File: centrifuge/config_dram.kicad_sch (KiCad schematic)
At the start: 4 parts

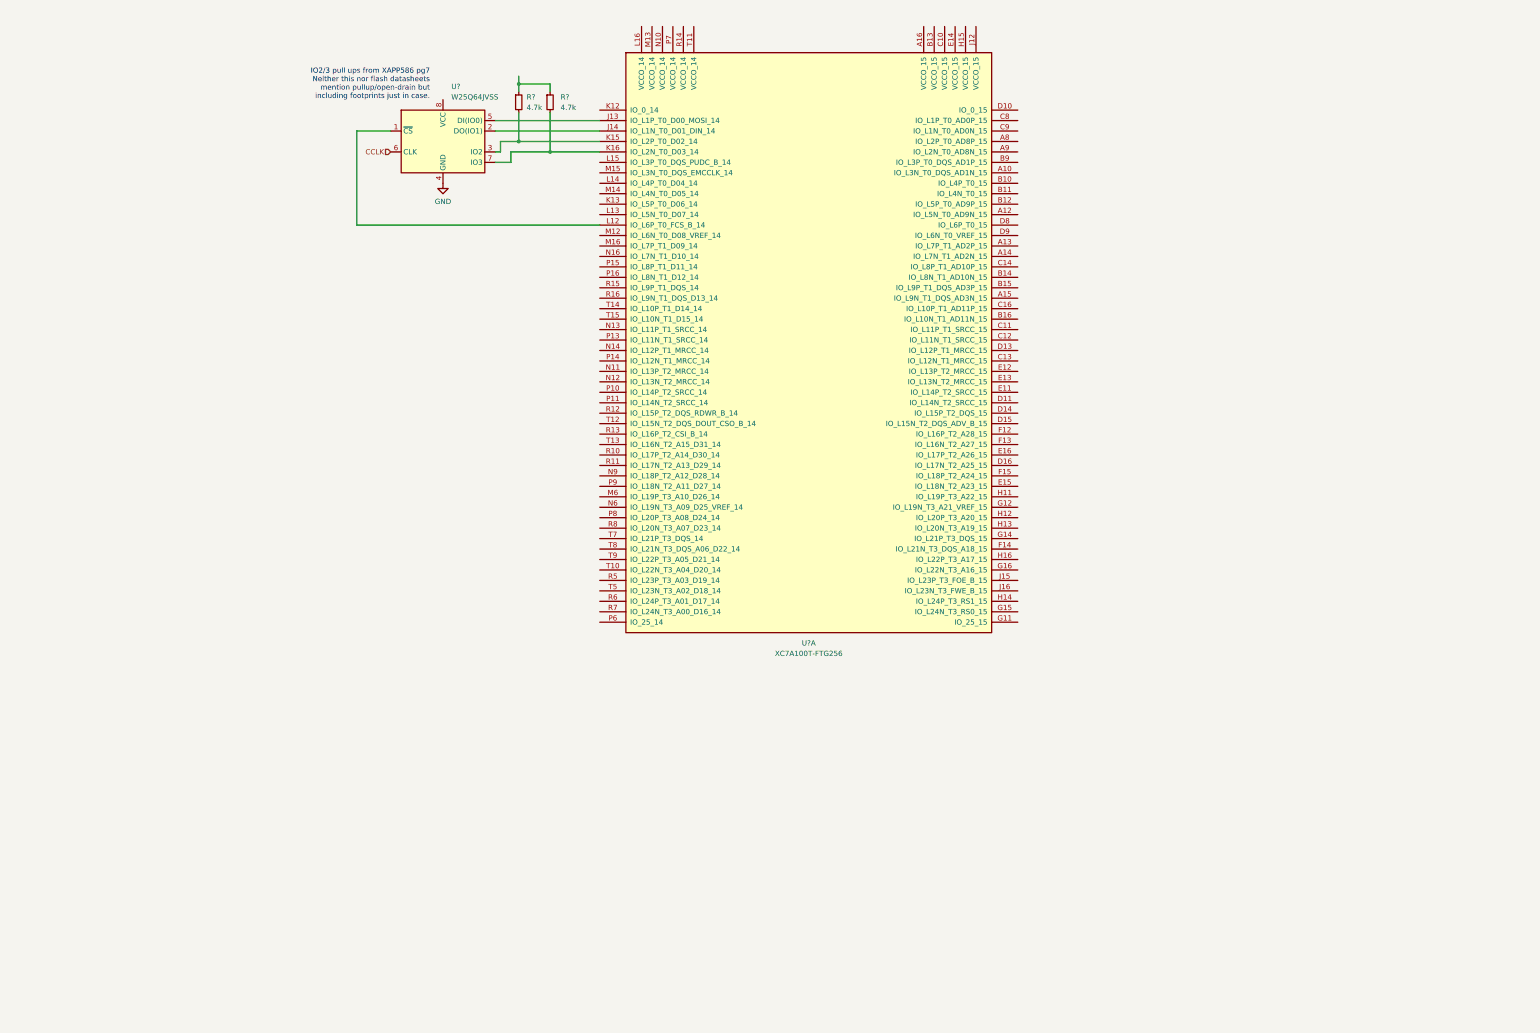
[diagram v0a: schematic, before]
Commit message: Made initial pin map of SRAM-FPGA and possible routing
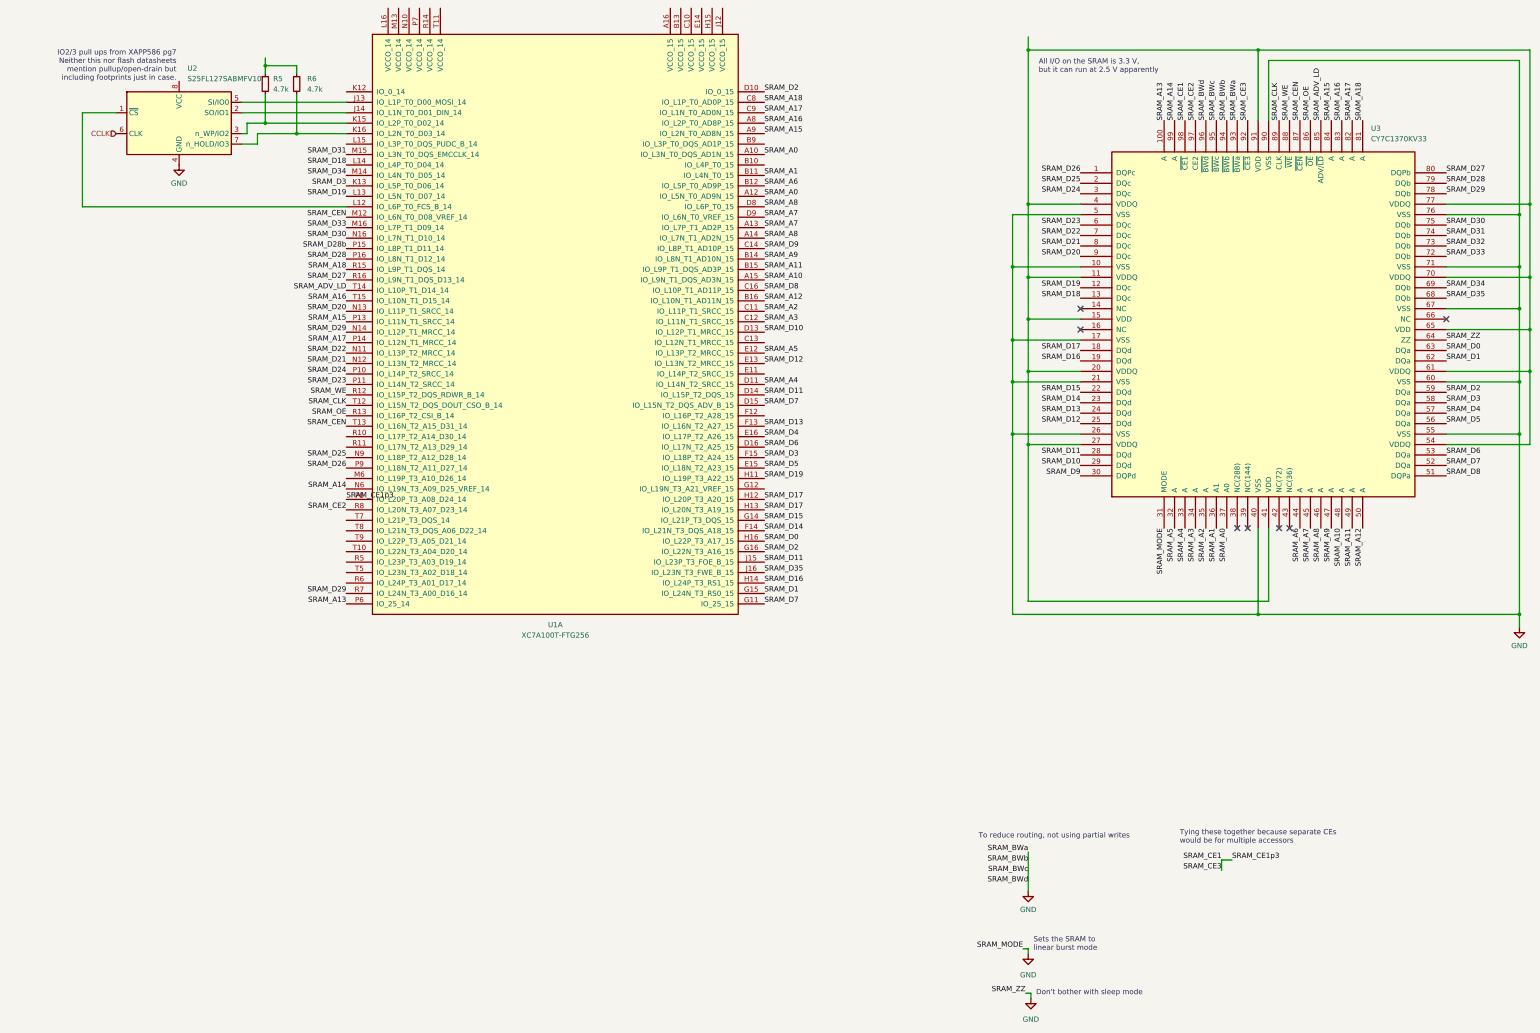
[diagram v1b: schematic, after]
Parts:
- added U3: CY7C1370KV33, Package_QFP:PQFP-100_14x20mm_P0.65mm, symbol centrifuge_symbols:CY7C1370KV33
- U1: renamed from U?; footprint (none) -> Package_BGA:Xilinx_FTG256
- U2: renamed from U?; value W25Q64JVSS -> S25FL127SABMFV10; symbol centrifuge_symbols:W25Q64JVSS -> centrifuge_symbols:S25FL127SABMFV10
- gave numbers to parts that had none: 2
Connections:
- net GND: now also U3.10 (VSS), U3.17 (VSS), U3.21 (VSS), U3.26 (VSS), U3.31 (MODE), U3.40 (VSS), U3.5 (VSS), U3.55 (VSS), U3.60 (VSS), U3.64 (ZZ), U3.67 (VSS), U3.71 (VSS), U3.76 (VSS), U3.90 (VSS), U3.93 (~{BWa}), U3.94 (~{BWb}), U3.95 (~{BWc}), U3.96 (~{BWd})
- net SRAM_A0: now reaches U1.A10 (IO_L3N_T0_DQS_AD1N_15)
- net SRAM_A0: now also U1.A12 (IO_L5N_T0_AD9N_15), U3.37 (A0)
- net SRAM_A7: now reaches U1.A13 (IO_L7P_T1_AD2P_15)
- net SRAM_A7: now also U1.D9 (IO_L6N_T0_VREF_15), U3.45 (A)
- net SRAM_A8: now reaches U1.A14 (IO_L7N_T1_AD2N_15)
- net SRAM_A8: now also U1.D8 (IO_L6P_T0_15), U3.46 (A)
- net SRAM_A10: now reaches U1.A15 (IO_L9N_T1_DQS_AD3N_15)
- net SRAM_A10: now also U3.48 (A)
- net SRAM_A16: now reaches U1.A8 (IO_L2P_T0_AD8P_15)
- net SRAM_A16: now also U1.T15 (IO_L10N_T1_D15_14), U3.83 (A)
- net SRAM_A15: now reaches U1.A9 (IO_L2N_T0_AD8N_15)
- net SRAM_A15: now also U1.P13 (IO_L11N_T1_SRCC_14), U3.84 (A)
- net SRAM_A1: now reaches U1.B11 (IO_L4N_T0_15)
- net SRAM_A1: now also U3.36 (A1)
- net SRAM_A6: now reaches U1.B12 (IO_L5P_T0_AD9P_15)
- net SRAM_A6: now also U3.44 (A)
- net SRAM_A9: now reaches U1.B14 (IO_L8N_T1_AD10N_15)
- net SRAM_A9: now also U3.47 (A)
- net SRAM_A11: now reaches U1.B15 (IO_L9P_T1_DQS_AD3P_15)
- net SRAM_A11: now also U3.49 (A)
- net SRAM_A12: now reaches U1.B16 (IO_L10N_T1_AD11N_15)
- net SRAM_A12: now also U3.50 (A)
- net SRAM_A2: now reaches U1.C11 (IO_L11P_T1_SRCC_15)
- net SRAM_A2: now also U3.35 (A)
- net SRAM_A3: now reaches U1.C12 (IO_L11N_T1_SRCC_15)
- net SRAM_A3: now also U3.34 (A)
- net SRAM_D9: now reaches U1.C14 (IO_L8P_T1_AD10P_15)
- net SRAM_D9: now also U3.30 (DQPd)
- net SRAM_D8: now reaches U1.C16 (IO_L10P_T1_AD11P_15)
- net SRAM_D8: now also U3.51 (DQPa)
- net SRAM_A18: now reaches U1.C8 (IO_L1P_T0_AD0P_15)
- net SRAM_A18: now also U1.R15 (IO_L9P_T1_DQS_14), U3.81 (A)
- net SRAM_A17: now reaches U1.C9 (IO_L1N_T0_AD0N_15)
- net SRAM_A17: now also U1.P14 (IO_L12N_T1_MRCC_14), U3.82 (A)
- net SRAM_D2: now reaches U1.D10 (IO_0_15)
- net SRAM_D2: now also U1.G16 (IO_L22N_T3_A16_15), U3.59 (DQa)
- net SRAM_A4: now reaches U1.D11 (IO_L14N_T2_SRCC_15)
- net SRAM_A4: now also U3.33 (A)
- net SRAM_D10: now reaches U1.D13 (IO_L12P_T1_MRCC_15)
- net SRAM_D10: now also U3.29 (DQd)
- net SRAM_D11: now reaches U1.D14 (IO_L15P_T2_DQS_15)
- net SRAM_D11: now also U1.J15 (IO_L23P_T3_FOE_B_15), U3.28 (DQd)
- net SRAM_D7: now reaches U1.D15 (IO_L15N_T2_DQS_ADV_B_15)
- net SRAM_D7: now also U1.G11 (IO_25_15), U3.52 (DQa)
- net SRAM_D6: now reaches U1.D16 (IO_L17N_T2_A25_15)
- net SRAM_D6: now also U3.53 (DQa)
- net SRAM_A5: now reaches U1.E12 (IO_L13P_T2_MRCC_15)
- net SRAM_A5: now also U3.32 (A)
- net SRAM_D12: now reaches U1.E13 (IO_L13N_T2_MRCC_15)
- net SRAM_D12: now also U3.25 (DQd)
- net SRAM_D5: now reaches U1.E15 (IO_L18N_T2_A23_15)
- net SRAM_D5: now also U3.56 (DQa)
- net SRAM_D4: now reaches U1.E16 (IO_L17P_T2_A26_15)
- net SRAM_D4: now also U3.57 (DQa)
- net SRAM_D13: now reaches U1.F13 (IO_L16N_T2_A27_15)
- net SRAM_D13: now also U3.24 (DQd)
- net SRAM_D14: now reaches U1.F14 (IO_L21N_T3_DQS_A18_15)
- net SRAM_D14: now also U3.23 (DQd)
- net SRAM_D3: now reaches U1.F15 (IO_L18P_T2_A24_15)
- net SRAM_D3: now also U1.K13 (IO_L5P_T0_D06_14), U3.58 (DQa)
- net SRAM_D15: now reaches U1.G14 (IO_L21P_T3_DQS_15)
- net SRAM_D15: now also U3.22 (DQd)
- net SRAM_D1: now reaches U1.G15 (IO_L24N_T3_RS0_15)
- net SRAM_D1: now also U3.62 (DQa)
- net SRAM_D19: now reaches U1.H11 (IO_L19P_T3_A22_15)
- net SRAM_D19: now also U1.L13 (IO_L5N_T0_D07_14), U3.12 (DQc)
- net SRAM_D17: now reaches U1.H12 (IO_L20P_T3_A20_15)
- net SRAM_D17: now also U1.H13 (IO_L20N_T3_A19_15), U3.18 (DQd)
- net SRAM_D16: now reaches U1.H14 (IO_L24P_T3_RS1_15)
- net SRAM_D16: now also U3.19 (DQd)
- net SRAM_D0: now reaches U1.H16 (IO_L22P_T3_A17_15)
- net SRAM_D0: now also U3.63 (DQa)
- net SRAM_D35: now reaches U1.J16 (IO_L23N_T3_FWE_B_15)
- net SRAM_D35: now also U3.68 (DQb)
- net SRAM_D18: now reaches U1.L14 (IO_L4P_T0_D04_14)
- net SRAM_D18: now also U3.13 (DQc)
- net SRAM_CEN: now reaches U1.M12 (IO_L6N_T0_D08_VREF_14)
- net SRAM_CEN: now also U1.T13 (IO_L16N_T2_A15_D31_14), U3.87 (~{CEN})
- net SRAM_D34: now reaches U1.M14 (IO_L4N_T0_D05_14)
- net SRAM_D34: now also U3.69 (DQb)
- net SRAM_D31: now reaches U1.M15 (IO_L3N_T0_DQS_EMCCLK_14)
- net SRAM_D31: now also U3.74 (DQb)
- net SRAM_D33: now reaches U1.M16 (IO_L7P_T1_D09_14)
- net SRAM_D33: now also U3.72 (DQb)
- net SRAM_D22: now reaches U1.N11 (IO_L13P_T2_MRCC_14)
- net SRAM_D22: now also U3.7 (DQc)
- net SRAM_D21: now reaches U1.N12 (IO_L13N_T2_MRCC_14)
- net SRAM_D21: now also U3.8 (DQc)
- net SRAM_D20: now reaches U1.N13 (IO_L11P_T1_SRCC_14)
- net SRAM_D20: now also U3.9 (DQc)
- net SRAM_D29: now reaches U1.N14 (IO_L12P_T1_MRCC_14)
- net SRAM_D29: now also U1.R7 (IO_L24N_T3_A00_D16_14), U3.78 (DQb)
- net SRAM_D30: now reaches U1.N16 (IO_L7N_T1_D10_14)
- net SRAM_D30: now also U3.75 (DQb)
- net SRAM_A14: now reaches U1.N6 (IO_L19N_T3_A09_D25_VREF_14)
- net SRAM_A14: now also U3.99 (A)
- net SRAM_D25: now reaches U1.N9 (IO_L18P_T2_A12_D28_14)
- net SRAM_D25: now also U3.2 (DQc)
- net SRAM_D24: now reaches U1.P10 (IO_L14P_T2_SRCC_14)
- net SRAM_D24: now also U3.3 (DQc)
- net SRAM_D23: now reaches U1.P11 (IO_L14N_T2_SRCC_14)
- net SRAM_D23: now also U3.6 (DQc)
- net SRAM_D28b: now reaches U1.P15 (IO_L8P_T1_D11_14)
- net SRAM_D28: now reaches U1.P16 (IO_L8N_T1_D12_14)
- net SRAM_D28: now also U3.79 (DQb)
- net SRAM_A13: now reaches U1.P6 (IO_25_14)
- net SRAM_A13: now also U3.100 (A)
- net SRAM_CE1: now reaches U1.P8 (IO_L20P_T3_A08_D24_14)
- net SRAM_CE1: now also U3.92 (~{CE3}), U3.98 (~{CE1})
- net SRAM_D26: now reaches U1.P9 (IO_L18N_T2_A11_D27_14)
- net SRAM_D26: now also U3.1 (DQPc)
- net SRAM_WE: now reaches U1.R12 (IO_L15P_T2_DQS_RDWR_B_14)
- net SRAM_WE: now also U3.88 (~{WE})
- net SRAM_OE: now reaches U1.R13 (IO_L16P_T2_CSI_B_14)
- net SRAM_OE: now also U3.86 (~{OE})
- net SRAM_D27: now reaches U1.R16 (IO_L9N_T1_DQS_D13_14)
- net SRAM_D27: now also U3.80 (DQPb)
- net SRAM_CE2: now reaches U1.R8 (IO_L20N_T3_A07_D23_14)
- net SRAM_CE2: now also U3.97 (CE2)
- net SRAM_CLK: now reaches U1.T12 (IO_L15N_T2_DQS_DOUT_CSO_B_14)
- net SRAM_CLK: now also U3.89 (CLK)
- net SRAM_ADV_LD: now reaches U1.T14 (IO_L10P_T1_D14_14)
- net SRAM_ADV_LD: now also U3.85 (ADV/~{LD})
- new net: U3.11 (VDDQ), U3.15 (VDD), U3.20 (VDDQ), U3.27 (VDDQ), U3.4 (VDDQ), U3.41 (VDD), U3.54 (VDDQ), U3.61 (VDDQ), U3.65 (VDD), U3.70 (VDDQ), U3.77 (VDDQ), U3.91 (VDD)
- new net SRAM_D32: U3.73 (DQb)
- no-connect marks 0 -> 7
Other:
- note added: "All I/O on the SRAM is 3.3 V, but it can run at 2.5 V apparently"
- note added: "Don't bother with sleep mode"
- note added: "Sets the SRAM to linear burst mode"
- note added: "To reduce routing, not using partial writes"
- note added: "Tying these together because separate CEs would be for multiple accessors"
- moved on the sheet: R5, R6, U1A, U2
